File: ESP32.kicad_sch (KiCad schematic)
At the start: 6 parts, among them U1 ESP32-C6-MINI-1

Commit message: update battery sense
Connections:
- net IO0 renamed BatSense
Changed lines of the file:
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@@
 	(wire
 		(pts
-			(xy 135.89 78.74) (xy 140.97 78.74)
+			(xy 135.89 78.74) (xy 147.32 78.74)
 		)
 		(stroke
@@
 			(effects
 				(font
+					(size 1.27 1.27)
+				)
+				(justify left)
+				(hide yes)
+			)
+		)
+	)
+	(global_label "BatSense"
+		(shape input)
+		(at 147.32 78.74 0)
+		(fields_autoplaced yes)
+		(effects
+			(font
+				(size 1.27 1.27)
+			)
+			(justify left)
+		)
+		(property "Intersheetrefs" "${INTERSHEET_REFS}"
+			(at 159.0137 78.74 0)
+			(effects
+				(font

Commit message: Create prelim PCB
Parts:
- C1, C2: value 0.1UF-0603-25V-(+80/-20%) -> 0.1uF
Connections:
- net IO1/V_BATT_2 is gone; now on net BNO_INT: U1.13 (XTAL_32K_N/IO1)
- net BNO_INT: no longer U1.5 (IO2)
- net BNO_CS renamed IO18/~{CS}
- net BNO_MOSI renamed IO19/SCK
- net BNO_RST renamed IO3
- net IO15/LP renamed IO15/LP
- new net BNO_INT2: U1.5 (IO2)
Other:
- moved on the sheet: C1, C2, R1, R2, RESET1

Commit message: Add status LED
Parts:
- added R8: 1k, Resistor_SMD:R_0402_1005Metric, symbol uSlime:R_US
- added STAT1: LED, LED_SMD:LED_0402_1005Metric, symbol uSlime:LED
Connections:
- net GND: now also R8.1
- net IO18/~{CS}: now also STAT1.2 (A)
- new net: R8.2, STAT1.1 (K)
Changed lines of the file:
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@@
 	(wire
 		(pts
-			(xy 134.62 118.11) (xy 137.16 118.11)
+			(xy 134.62 118.11) (xy 144.78 118.11)
 		)
 		(stroke
@@
 	)
 	(symbol
+		(lib_id "power:GND")
+		(at 152.4 125.73 0)
+		(unit 1)
+		(exclude_from_sim no)
+		(in_bom yes)
+		(on_board yes)
+		(dnp no)
+		(property "Reference" "#GND01"
+			(at 152.4 125.73 0)
+			(effects
+				(font
+					(size 1.27 1.27)
+				)
+				(hide yes)
+			)
+		)
+		(property "Value" "GND"
+			(at 152.4 129.794 0)
+			(effects
+				(font
+					(size 1.778 1.778)
+				)
+				(justify top)
+			)
+		)
+		(property "Footprint" ""
+			(at 152.4 125.73 0)
+			(effects
+				(font
+					(size 1.27 1.27)
+				)
+				(hide yes)
+			)
+		)
+		(property "Datasheet" ""
+			(at 152.4 125.73 0)
+			(effects
+				(font
+					(size 1.27 1.27)
+				)
+				(hide yes)
+			)
+		)
+		(property "Description" "Power symbol creates a global label with name \"GND\" , ground"
+			(at 152.4 125.73 0)
+			(effects
+				(font
+					(size 1.27 1.27)
+				)
+				(hide yes)
+			)
+		)
+		(pin "1"
+		)
+		(instances
+			(project "uSlime"
+				(path "/f32c1c49-f803-4e7c-a530-6db148a7ba36/27e9da7b-3bfa-4574-a980-93f02fcd8fa2"
+					(reference "#GND01")
+					(unit 1)
+				)
+			)
+		)
+	)
+	(symbol
 		(lib_id "uSlime:R_US")
 		(at 170.18 97.79 180)
@@
 				(path "/f32c1c49-f803-4e7c-a530-6db148a7ba36/27e9da7b-3bfa-4574-a980-93f02fcd8fa2"
 					(reference "R2")
+					(unit 1)
+				)
+			)
+		)
+	)
+	(symbol
+		(lib_id "uSlime:LED")
+		(at 148.59 118.11 180)
+		(unit 1)
+		(exclude_from_sim no)
+		(in_bom yes)
+		(on_board yes)
+		(dnp no)
+		(property "Reference" "STAT1"
+			(at 146.304 114.046 0)
+			(effects
+				(font
+					(size 1.27 1.27)
+				)
+				(justify right)
+			)
+		)
+		(property "Value" "LED"
+			(at 146.812 115.824 0)
+			(effects
+				(font
+					(size 1.27 1.27)
+				)
+				(justify right)
+			)
+		)
+		(property "Footprint" "LED_SMD:LED_0402_1005Metric"
+			(at 148.59 118.11 0)
+			(effects
+				(font
+					(size 1.27 1.27)
+				)
+				(hide yes)
+			)
+		)
+		(property "Datasheet" "~"
+			(at 148.59 118.11 0)
+			(effects
+				(font
+					(size 1.27 1.27)
+				)
+				(hide yes)
+			)
+		)
+		(property "Description" "Light emitting diode"
+			(at 148.59 118.11 0)
+			(effects
+				(font
+					(size 1.27 1.27)
+				)
+				(hide yes)
+			)
+		)
+		(pin "1"
+		)
+		(pin "2"
+		)
+		(instances
+			(project "uSlime"
+				(path "/f32c1c49-f803-4e7c-a530-6db148a7ba36/27e9da7b-3bfa-4574-a980-93f02fcd8fa2"
+					(reference "STAT1")
 					(unit 1)
 				)
@@
 					(unit 1)
 				)
+			)
+		)
+	)
+	(symbol
+		(lib_id "uSlime:R_US")
+		(at 152.4 121.92 180)
+		(unit 1)
+		(exclude_from_sim no)
+		(in_bom yes)
+		(on_board yes)
+		(dnp no)
+		(fields_autoplaced yes)
+		(property "Reference" "R8"
+			(at 154.94 120.6499 0)
+			(effects
+				(font
+					(size 1.27 1.27)
+				)
+				(justify right)
+			)
+		)
+		(property "Value" "1k"
+			(at 154.94 123.1899 0)
+			(effects
+				(font
+					(size 1.27 1.27)
+				)
+				(justify right)
+			)
+		)
+		(property "Footprint" "Resistor_SMD:R_0402_1005Metric"
+			(at 151.384 121.666 90)
+			(effects
+				(font
+					(size 1.27 1.27)
+				)
+				(hide yes)
+			)
+		)
+		(property "Datasheet" "~"
+			(at 152.4 121.92 0)
+			(effects
+				(font
+					(size 1.27 1.27)
+				)
+				(hide yes)
+			)
+		)
+		(property "Description" "Resistor, US symbol"
+			(at 152.4 121.92 0)
+			(effects
+				(font
+					(size 1.27 1.27)
+				)
+				(hide yes)
+			)
+		)
+		(pin "2"
+		)
+		(pin "1"
+		)
+		(instances
+			(project "uSlime"
+				(path "/f32c1c49-f803-4e7c-a530-6db148a7ba36/27e9da7b-3bfa-4574-a980-93f02fcd8fa2"
+					(reference "R8")
+					(unit 1)
+				)

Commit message: 2nd version but smaller at 25x28
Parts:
- renumbered RESET1 to RESET, STAT1 to STAT
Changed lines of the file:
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@@
 		(on_board yes)
 		(dnp no)
-		(property "Reference" "RESET1"
+		(property "Reference" "RESET"
 			(at 159.004 112.014 90)
 			(effects
@@
 			(project "uSlime"
 				(path "/f32c1c49-f803-4e7c-a530-6db148a7ba36/27e9da7b-3bfa-4574-a980-93f02fcd8fa2"
-					(reference "RESET1")
+					(reference "RESET")
 					(unit 1)
 				)
@@
 		(on_board yes)
 		(dnp no)
-		(property "Reference" "STAT1"
+		(property "Reference" "STAT"
 			(at 146.304 114.046 0)
 			(effects
@@
 			(project "uSlime"
 				(path "/f32c1c49-f803-4e7c-a530-6db148a7ba36/27e9da7b-3bfa-4574-a980-93f02fcd8fa2"
-					(reference "STAT1")
-					(unit 1)
-				)
+					(reference "STAT")
+					(unit 1)
+				)

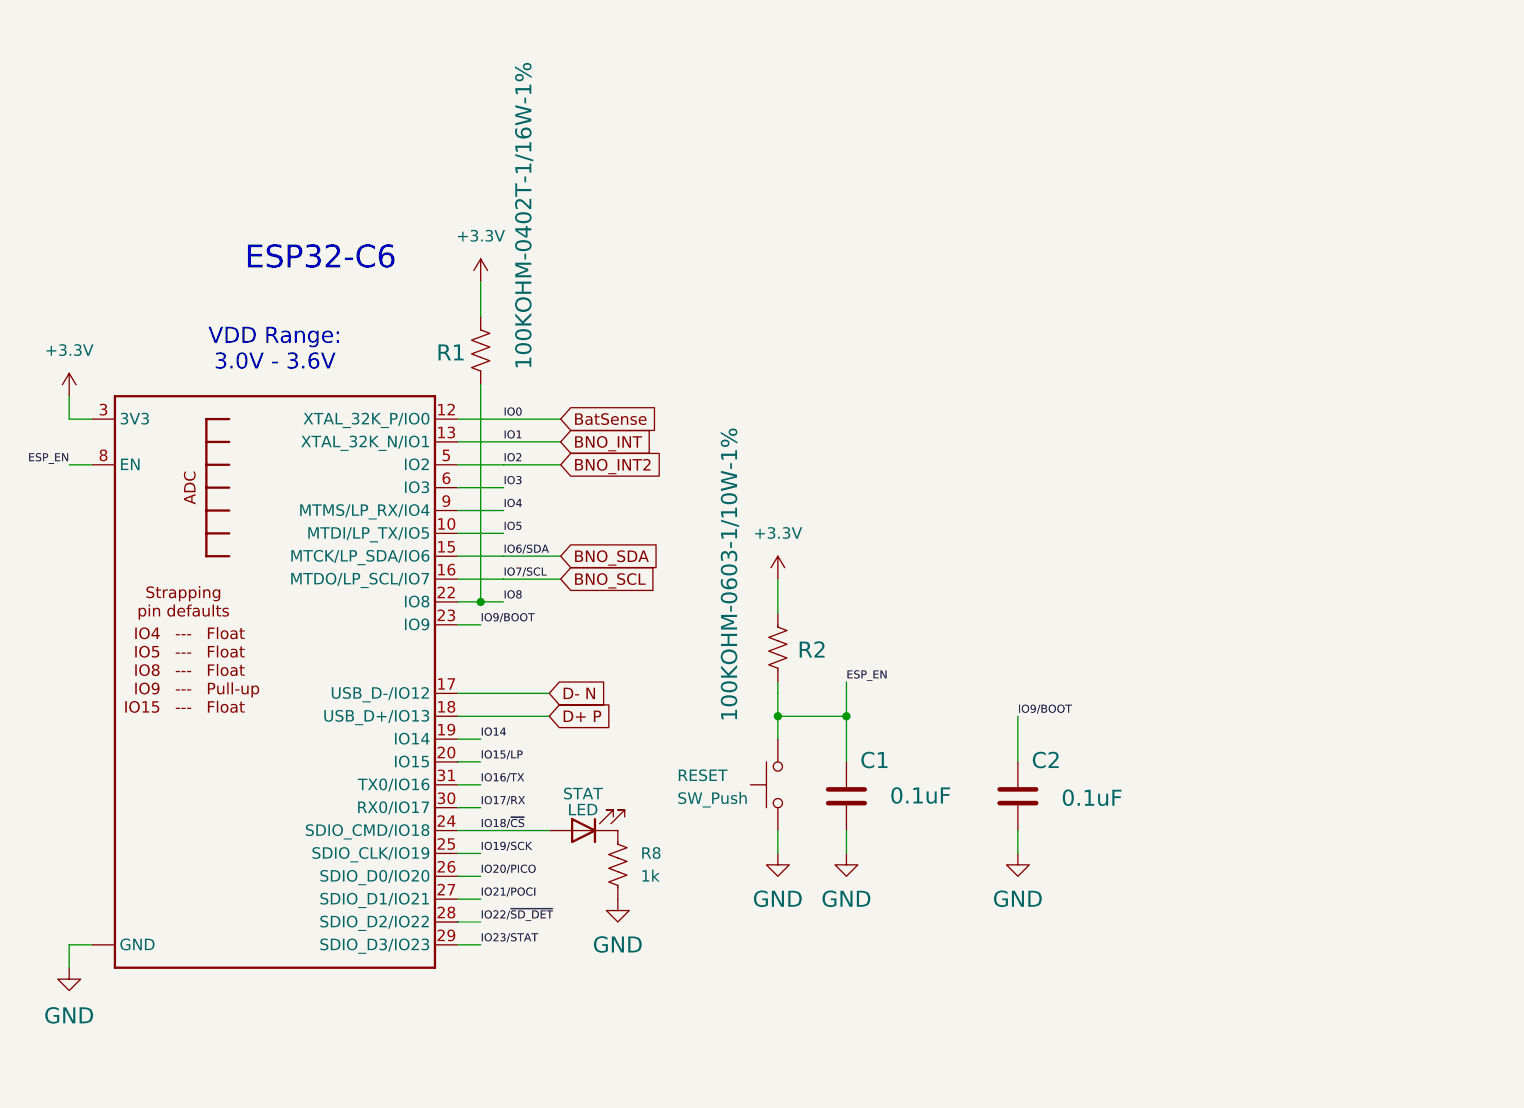
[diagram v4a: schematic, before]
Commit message: Add logo and remove crystal
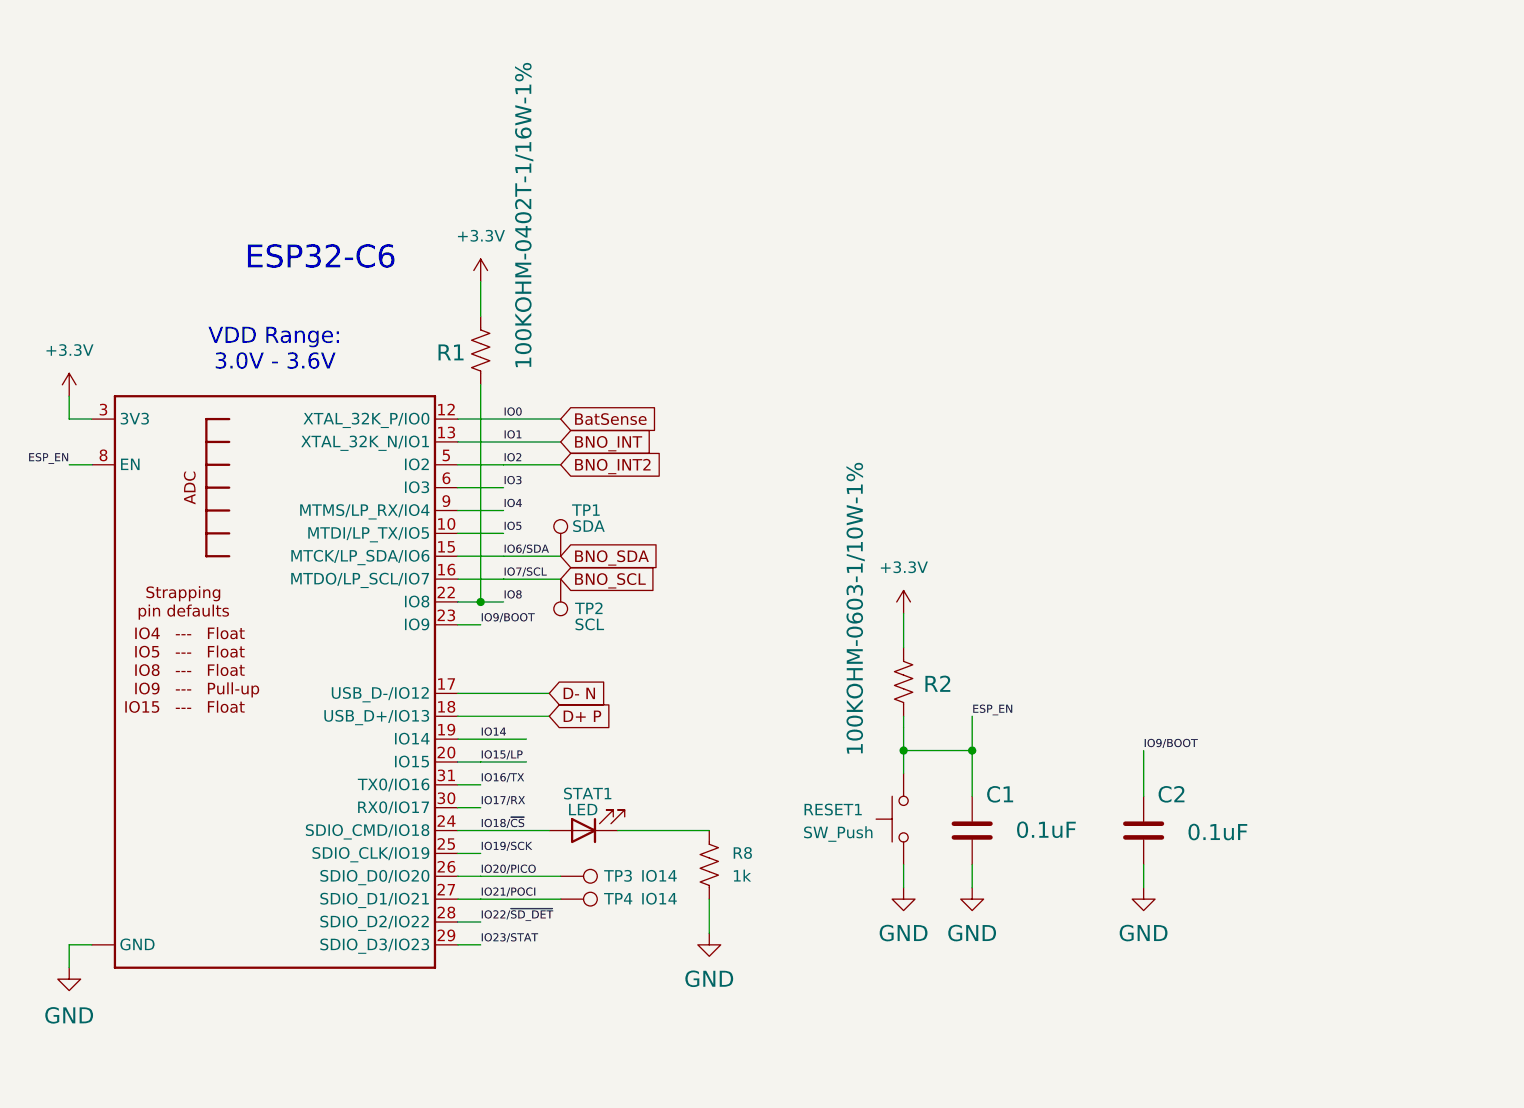
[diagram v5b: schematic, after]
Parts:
- added TP1: SDA, TestPoint:TestPoint_Pad_2.0x2.0mm, symbol uSlime:TestPoint
- added TP2: SCL, TestPoint:TestPoint_Pad_2.0x2.0mm, symbol uSlime:TestPoint
- added TP3, TP4: IO14, TestPoint:TestPoint_Pad_2.0x2.0mm, symbol uSlime:TestPoint
- renumbered RESET to RESET1, STAT to STAT1
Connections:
- net BNO_SCL: now also TP2.1
- net BNO_SDA: now also TP1.1
- net IO20/PICO: now also TP3.1
- net IO21/POCI: now also TP4.1
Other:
- moved on the sheet: C1, C2, R2, R8, RESET1

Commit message: Revamp pwr resistor, cap placement, fix switch sym
Fix placement of resistors and capacitor placement b/c additional
components were added to power circuit and weren't correct...

Also fixed switch symbol so wires actually connect to it in schematic
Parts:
- R1: value 100KOHM-0402T-1/16W-1% -> 100k
- R2: value 100KOHM-0603-1/10W-1% -> 100k
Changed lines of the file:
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@@
 			)
 		)
-		(property "Value" "100KOHM-0603-1/10W-1%"
-			(at 179.832 93.472 90)
+		(property "Value" "100k"
+			(at 182.372 101.6 90)
 			(effects
 				(font
@@
 			)
 		)
-		(property "Value" "100KOHM-0402T-1/16W-1%"
-			(at 143.002 49.784 90)
-			(effects
-				(font
+		(property "Value" "100k"
+			(at 141.478 64.77 90)
+			(effects
+				(font
